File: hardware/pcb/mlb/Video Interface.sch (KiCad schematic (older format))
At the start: 20 parts

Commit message: Import to newer KiCad version.
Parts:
- UK6: symbol Memory_EPROM:2764 -> Macintosh-SE30-Main-Logic-Board-rescue:2764-Memory_EPROM
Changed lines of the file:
@@
 EESchema Schematic File Version 4
+LIBS:Macintosh SE30 Main Logic Board-cache
 EELAYER 30 0
 EELAYER END
@@
 Connection ~ 7250 2650
 $Comp
-L Memory_EPROM:2764 UK6
+L Macintosh-SE30-Main-Logic-Board-rescue:2764-Memory_EPROM UK6
 U 1 1 5ED23C7D
 P 3650 6850

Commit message: Fix errors found in review of the Macintosh SE/30 schematic redraw.
Page 1:

* DSACK*(0:1) (syntax)
* R-W* (inconsistent syntax)
* IPL different syntax
* PDS 38, C16M not grounded
* PDS 39, should be grounded

Page 2:

* RAAF*(8), RABF*(9), RAAF*(10), RABF*(10) (syntax)
* RCMUX* (syntax)
* ROM* missing page 3 indicator
* ROMSIMM1 GND 10, 30, 64
* ROMSIMM1 Incorrect +5V lines
* ROMSIMM1 Confusing bus line drawing angles makes connections look
  duplicated

Page 3:

* VIAIRQ2* (syntax)
* VIAIRQ1N (syntax, on GLUE template)
* SCCRD* (syntax)

Page 4:

* VIA template, RS0, RS1, RS2, RS3 erroneously written as R50, R51,
  R52, R53
* V1PB7 erroneously written as VIPB7
* RTC-D erroneously written as RTC-O
* V1PA0, V1PA1, V1PA2 erroneously written as VIPA0, VIPA1, VIPA2
* warning: additional label BATT not present
* UL11 ADB template, P5 erroneously written as P2
* ADBO erroneously written as ADB0
* SNDINT* erroneously written as SNTINT*

Page 5:

* HSYNC* on UG7 (syntax)
* UJ6 confusing bus line makes signals look duplicated
* Video ROM UK6 not labeled with reference designator (already inside
  KiCad file, stale PDF?)
* VIDS4, VIDS3, VIDS2, VIDS1, VIDS0 erroneously written a VID54,
  VID53, VID53, VID51, VID50
* R-W* alternate page reference erroneously written as RW*
* 74F253 template, G erroneously labeled as GND
* 74F253 template, missing second G enable pin
* style: C0 in 74F253 template should not be C0(GND)
* warning: UA8 ALTVID line could have another label close to the chip

Page 6:

* warning: On SWIM, WRDATA could have label WR*
* DB25 connector: DP*, DB0*, DB1*, DB2*, DB3*, DB4*, DB5*, DB6*, DB7*
  (syntax)
* J8 Ribbon Connector: Missing +12V on 13, 15, 17, 19
* J6 DB-19: Missing +12V-DSK on 7, 8
* warning: missing RDDATA.F additional label near J6 DB-19 pin 18
* warning: missing WRITE.F additional label near J6 DB-19 pin 19
* warning: confusing bus line layout on 53C80 looks like duplicate
  wiring

Page 7:

* RXDA+ erroneously written as RXDB+
* HSKOA erroneo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
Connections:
- net labels added: R-W*, VIDS0, VIDS1, VIDS2, VIDS3, VIDS4
- net labels removed: HSYNC, RW*, VID50, VID51, VID52, VID53, VID54
- wire segments 436 -> 432
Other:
- moved on the sheet: UA8, UC8

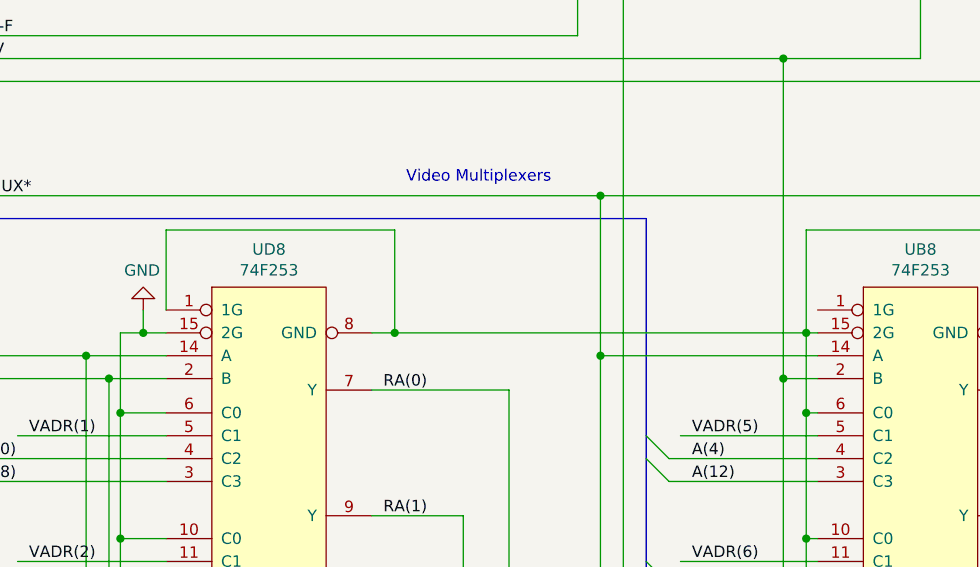
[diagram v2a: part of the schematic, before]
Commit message: Fix some minor errors found from review of desired changes.
* DSACK*(0:1) (syntax)

* Wires wrong on redraw of 74F253 template.
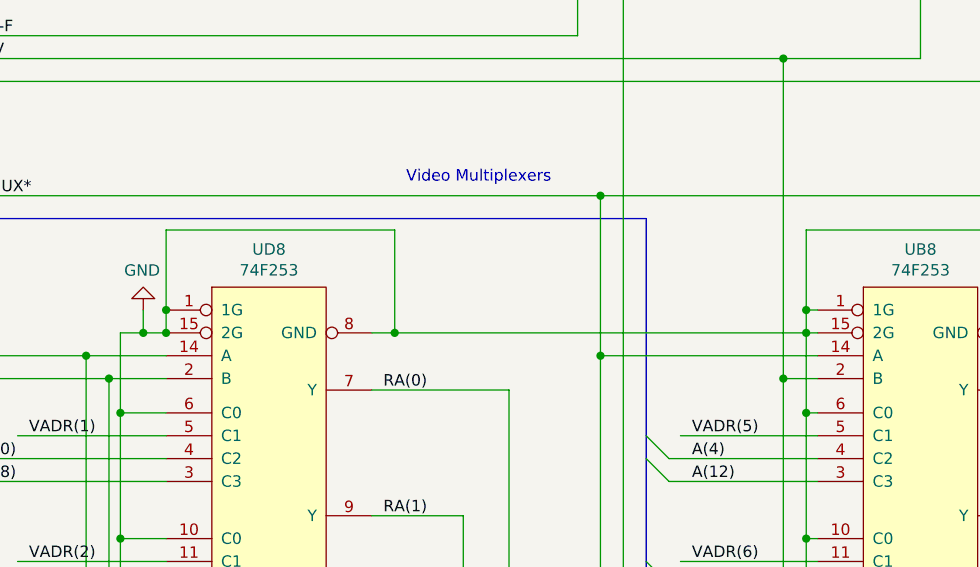
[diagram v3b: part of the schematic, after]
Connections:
- net GND: now also UA8.1 (1G), UA8.15 (2G), UA8.8 (GND), UB8.1 (1G), UB8.10 (C0), UB8.15 (2G), UB8.6 (C0), UB8.8 (GND), UD8.1 (1G), UD8.8 (GND)
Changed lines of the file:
@@
 Connection ~ 6950 5700
 Wire Wire Line
-	8750 5700 8750 5250
+	8750 5700 8750 5600
 Wire Wire Line
 	8750 5250 9950 5250
@@
 Wire Wire Line
 	10200 7750 10200 6800
-Wire Wire Line
-	7950 8500 8800 8500
-Wire Bus Line
-	15800 5050 15800 7800
-Wire Bus Line
-	13450 3400 13450 5050
-Wire Bus Line
-	15650 6200 15650 9200
-Wire Bus Line
-	4550 6150 4550 9200
-Wire Bus Line
-	8050 5200 8050 8600
-Wire Bus Line
-	5000 5200 5000 8600
-Wire Bus Line
-	2450 3900 2450 5200
-Wire Bus Line
-	2450 5200 2450 7350
 Text Label 8250 8500 0    50   ~ 0
 ALTVID
+Wire Wire Line
+	5950 5600 5950 5700
+Connection ~ 5950 5600
+Connection ~ 5950 5700
+Wire Wire Line
+	8800 5600 8750 5600
+Wire Wire Line
+	7950 8500 8800 8500
+Wire Bus Line
+	15800 5050 15800 7800
+Wire Bus Line
+	13450 3400 13450 5050
+Wire Bus Line
+	15650 6200 15650 9200
+Wire Bus Line
+	4550 6150 4550 9200
+Wire Bus Line
+	8050 5200 8050 8600
+Wire Bus Line
+	5000 5200 5000 8600
+Wire Bus Line
+	2450 3900 2450 5200
+Wire Bus Line
+	2450 5200 2450 7350
+Connection ~ 8750 5600
+Wire Wire Line
+	8750 5600 8750 5250
 $EndSCHEMATC
